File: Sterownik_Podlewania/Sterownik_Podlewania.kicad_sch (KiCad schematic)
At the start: 1 part, among them U1 ESP32-DEVKITC

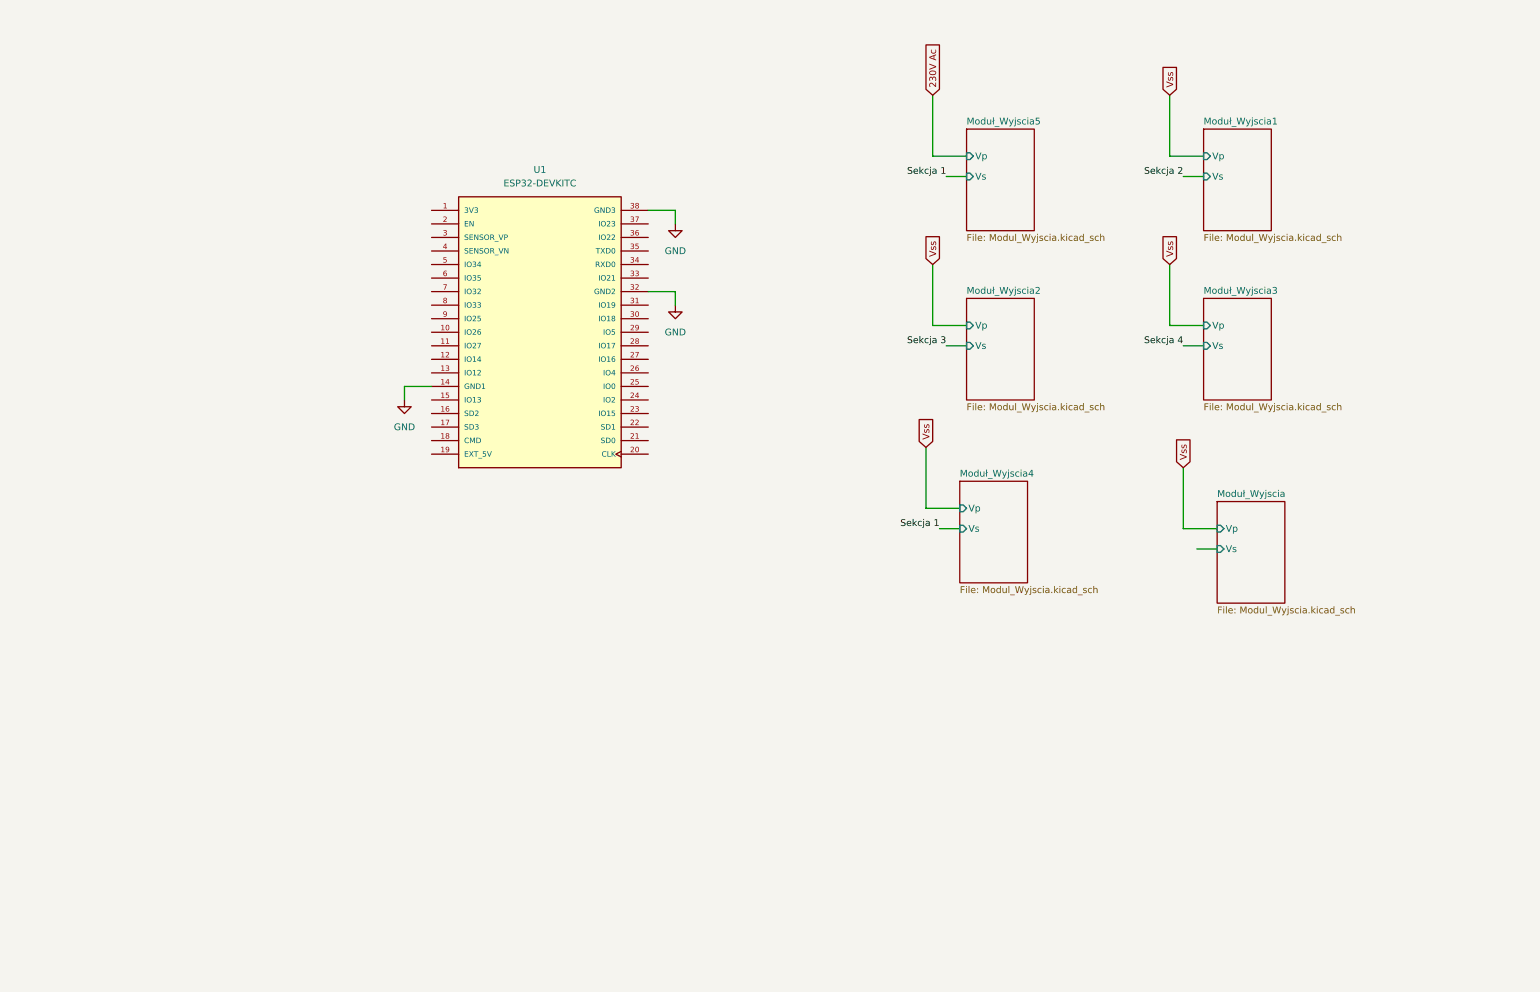
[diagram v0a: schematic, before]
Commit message: Dodanie zasilania, sekcji czujników światła, modyfikacja przełączników, dodanie znaczników
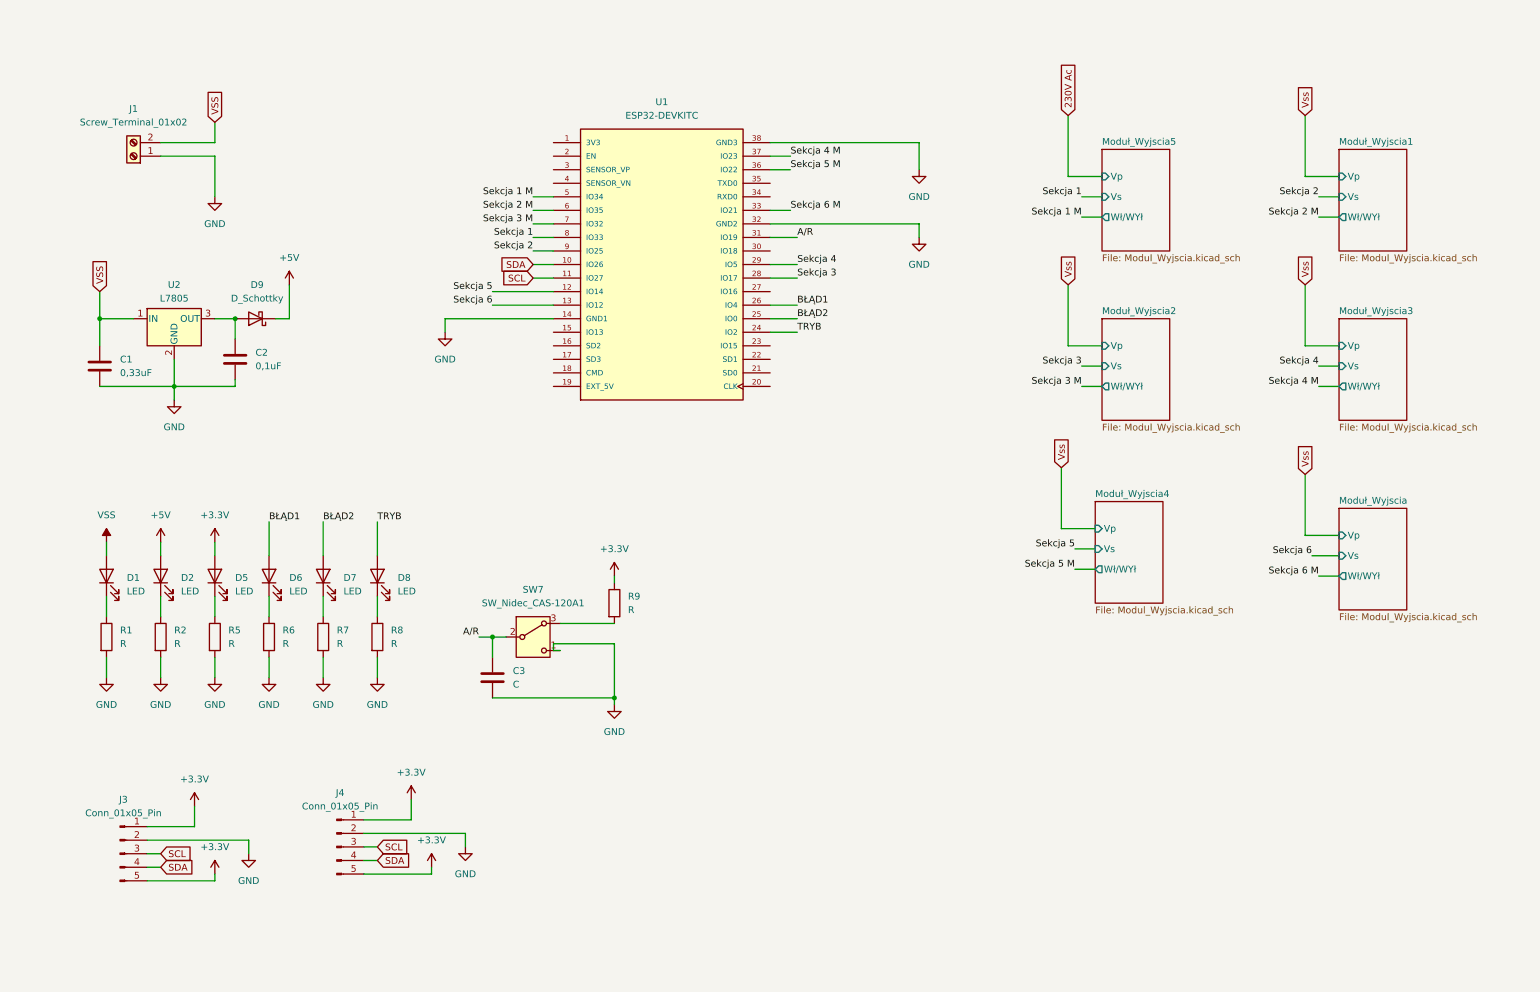
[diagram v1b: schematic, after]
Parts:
- added C1: 0,33uF, symbol Device:C
- added C2: 0,1uF, symbol Device:C
- added C3: C, symbol Device:C
- added D1, D2, D5, D6, D7, D8: LED, symbol Device:LED
- added D9: D_Schottky, symbol Device:D_Schottky
- added J1: Screw_Terminal_01x02, symbol Connector:Screw_Terminal_01x02
- added J3, J4: Conn_01x05_Pin, symbol Connector:Conn_01x05_Pin
- added R1, R2, R5, R6, R7, R8, R9: R, symbol Device:R
- added SW7: SW_Nidec_CAS-120A1, Button_Switch_SMD:Nidec_Copal_CAS-120A, symbol Switch:SW_Nidec_CAS-120A1
- added U2: L7805, symbol Regulator_Linear:L7805
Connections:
- net GND: now also C1.2, C2.2, C3.2, J1.1 (Pin_1), J3.2 (Pin_2), J4.2 (Pin_2), R1.2, R2.2, R5.2, R6.2, R7.2, R8.2, SW7.1 (C), U2.2 (GND)
- net Sekcja 1: now also U1.8 (IO33)
- net Sekcja 2: now also U1.9 (IO25)
- net Sekcja 3: now also U1.28 (IO17)
- net Sekcja 4: now also U1.29 (IO5)
- net SDA: now reaches U1.10 (IO26)
- net SDA: now also J3.4 (Pin_4), J4.4 (Pin_4)
- net SCL: now reaches U1.11 (IO27)
- net SCL: now also J3.3 (Pin_3), J4.3 (Pin_3)
- net Sekcja 5: now reaches U1.12 (IO14)
- net Sekcja 6: now reaches U1.13 (IO12)
- net TRYB: now reaches U1.24 (IO2)
- net TRYB: now also D8.2 (A)
- net BŁĄD2: now reaches U1.25 (IO0)
- net BŁĄD2: now also D7.2 (A)
- net BŁĄD1: now reaches U1.26 (IO4)
- net BŁĄD1: now also D6.2 (A)
- net A/R: now reaches U1.31 (IO19)
- net A/R: now also C3.1, SW7.2 (B)
- net Sekcja 6 M: now reaches U1.33 (IO21)
- net Sekcja 5 M: now reaches U1.36 (IO22)
- net Sekcja 4 M: now reaches U1.37 (IO23)
- net Sekcja 1 M: now reaches U1.5 (IO34)
- net Sekcja 2 M: now reaches U1.6 (IO35)
- net Sekcja 3 M: now reaches U1.7 (IO32)
- new net: D7.1 (K), R7.1
- new net: C2.1, D9.2 (A), U2.3 (OUT)
- new net: D2.1 (K), R2.1
- new net: D6.1 (K), R6.1
- new net: D5.1 (K), R5.1
- new net: R9.2, SW7.3 (A)
- new net: D8.1 (K), R8.1
- new net: D1.1 (K), R1.1
- new net +3.3V: D5.2 (A), J3.1 (Pin_1), J3.5 (Pin_5), J4.1 (Pin_1), J4.5 (Pin_5), R9.1
- new net +5V: D2.2 (A), D9.1 (K)
- new net VSS: C1.1, D1.2 (A), J1.2 (Pin_2), U2.1 (IN)
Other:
- sheet Moduł_Wyjscia ports: added Wł/WYł; removed none
- sheet Moduł_Wyjscia1 ports: added Wł/WYł; removed none
- sheet Moduł_Wyjscia2 ports: added Wł/WYł; removed none
- sheet Moduł_Wyjscia3 ports: added Wł/WYł; removed none
- sheet Moduł_Wyjscia4 ports: added Wł/WYł; removed none
- sheet Moduł_Wyjscia5 ports: added Wł/WYł; removed none
- moved on the sheet: U1

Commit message: Modyfikacja sekcji czujników
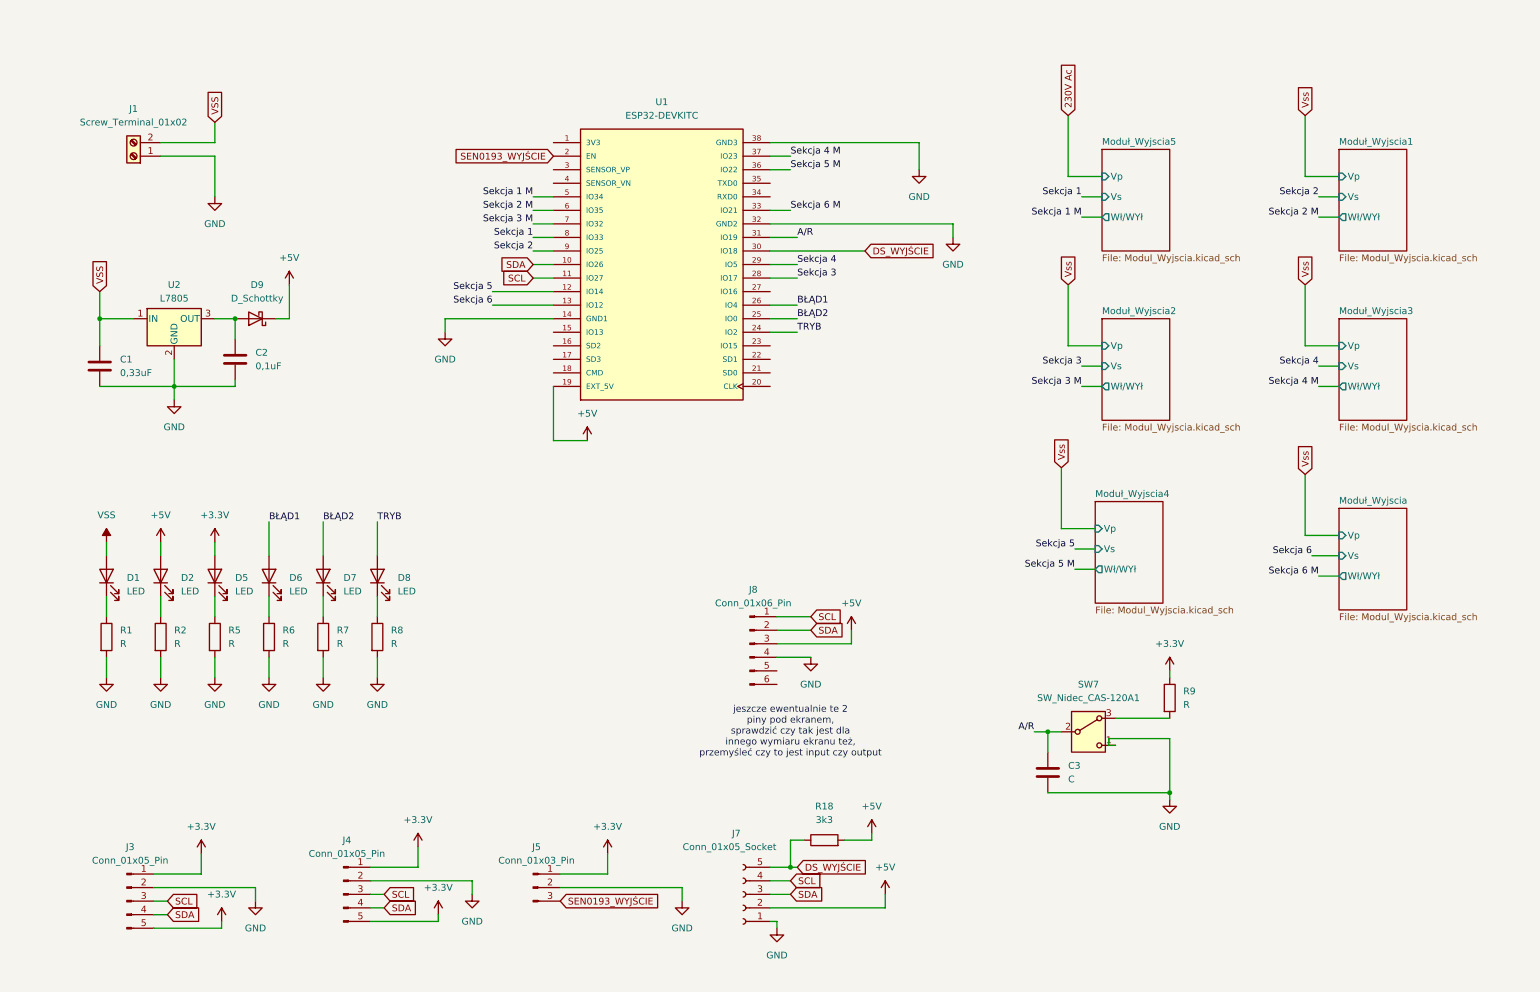
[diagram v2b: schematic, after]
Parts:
- added J5: Conn_01x03_Pin, symbol Connector:Conn_01x03_Pin
- added J7: Conn_01x05_Socket, symbol Connector:Conn_01x05_Socket
- added J8: Conn_01x06_Pin, symbol Connector:Conn_01x06_Pin
- added R18: 3k3, symbol Device:R
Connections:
- net +3.3V: now also J5.1 (Pin_1)
- net +5V: now also U1.19 (EXT_5V), J7.2 (Pin_2), J8.3 (Pin_3), R18.2
- net GND: now also J5.2 (Pin_2), J7.1 (Pin_1), J8.4 (Pin_4)
- net SCL: now also J7.4 (Pin_4), J8.1 (Pin_1)
- net SDA: now also J7.3 (Pin_3), J8.2 (Pin_2)
- net SEN0193_WYJŚCIE: now reaches U1.2 (EN)
- net SEN0193_WYJŚCIE: now also J5.3 (Pin_3)
- net DS_WYJŚCIE: now reaches U1.30 (IO18)
- net DS_WYJŚCIE: now also J7.5 (Pin_5), R18.1
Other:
- note added: "jeszcze ewentualnie te 2 piny pod ekranem, sprawdzić czy tak jest dla innego wymiaru ekranu też, przemyśleć czy to jest input czy output"
- moved on the sheet: C3, J3, J4, R9, SW7

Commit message: Dodanie adresów I2C, linków, czujnika temp, konwerter poziomów napięć
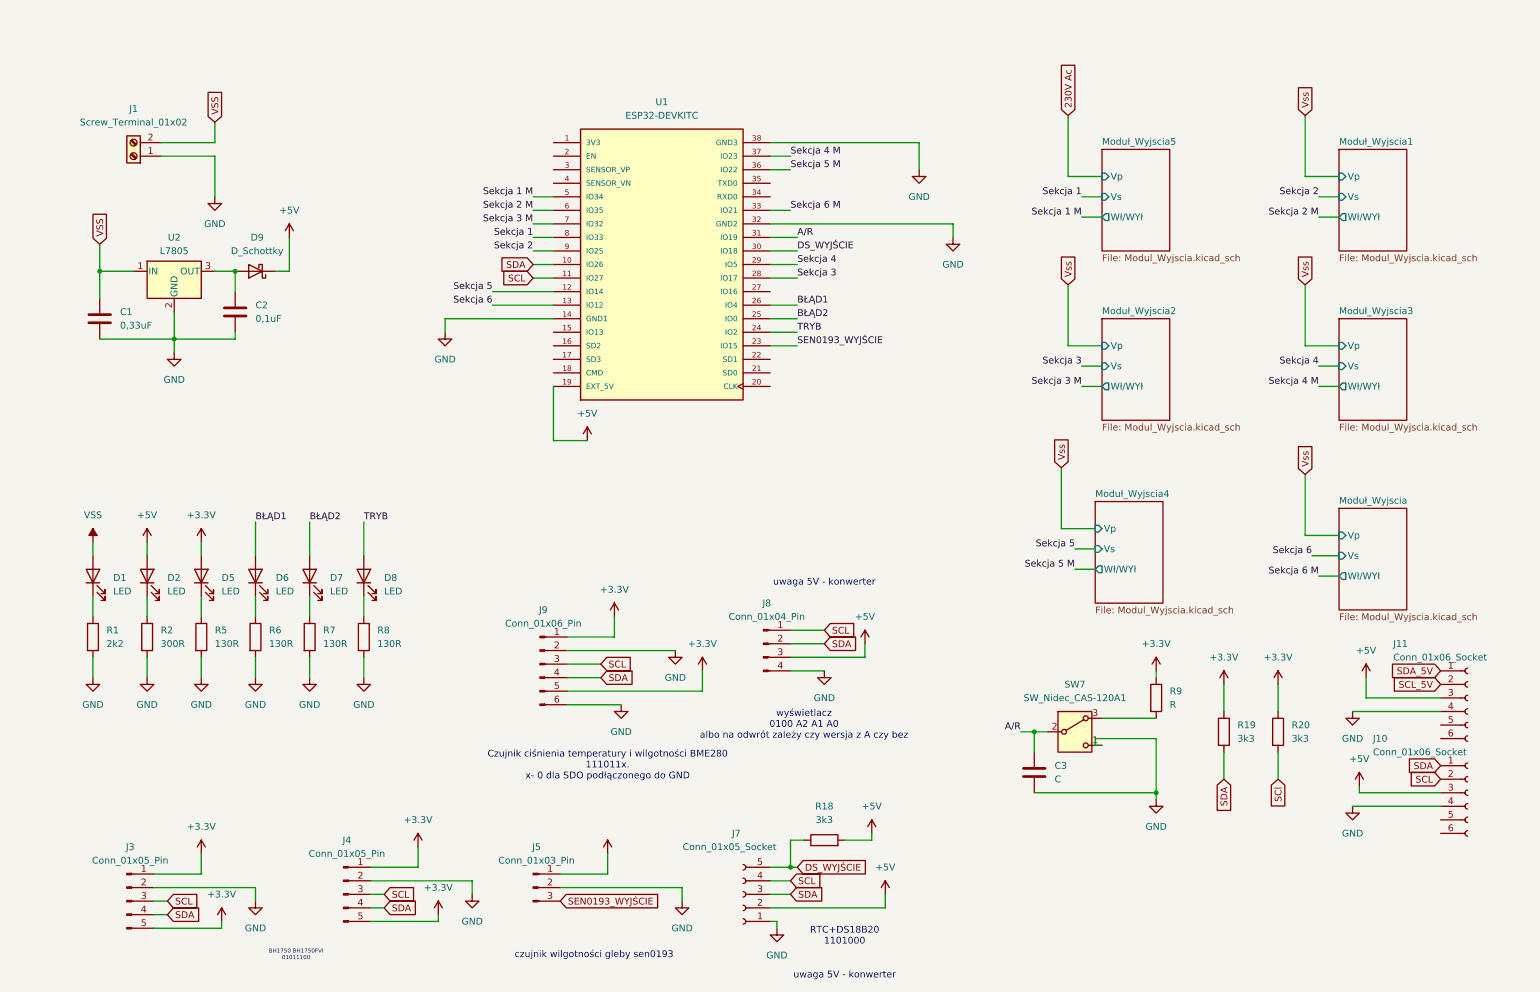
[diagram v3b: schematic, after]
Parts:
- removed J8: Conn_01x06_Pin, symbol Connector:Conn_01x06_Pin
- added J10, J11: Conn_01x06_Socket, symbol Connector:Conn_01x06_Socket
- added J8: Conn_01x04_Pin, symbol Connector:Conn_01x04_Pin
- added J9: Conn_01x06_Pin, symbol Connector:Conn_01x06_Pin
- added R19, R20: 3k3, symbol Device:R
- R1: value R -> 2k2
- R2: value R -> 300R
- R5, R6, R7, R8: value R -> 130R
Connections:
- net +3.3V: now also J9.1 (Pin_1), J9.5 (Pin_5), R19.1, R20.1
- net +5V: now also J10.3 (Pin_3), J11.3 (Pin_3), J8.3 (Pin_3)
- net GND: now also J10.4 (Pin_4), J11.4 (Pin_4), J8.4 (Pin_4), J9.2 (Pin_2), J9.6 (Pin_6)
- net SCL: now also J10.2 (Pin_2), J8.1 (Pin_1), J9.3 (Pin_3)
- net SDA: now also J10.1 (Pin_1), J8.2 (Pin_2), J9.4 (Pin_4), R19.2
- net SEN0193_WYJŚCIE: now also U1.23 (IO15); no longer U1.2 (EN)
- new net SCL_5V: J11.2 (Pin_2)
- new net SCl: R20.2
- new net SDA_5V: J11.1 (Pin_1)
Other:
- note added: "BH1750 BH1750FVI 01011100"
- note added: "Czujnik ciśnienia temperatury i wilgotności BME280 111011x. x- 0 dla SDO podłączonego do GND"
- note added: "RTC+DS18B20 1101000"
- note added: "czujnik wilgotności gleby sen0193"
- note added: "uwaga 5V - konwerter"
- note added: "wyświetlacz 0100 A2 A1 A0 albo na odwrót zależy czy wersja z A czy bez"
- note removed: "jeszcze ewentualnie te 2 piny pod ekranem, sprawdzić czy tak jest dla innego wymiaru ekranu też, przemyśleć czy to jest input czy output"
- moved on the sheet: C1, C2, C3, D1, D2, D5, D6, D7, D8, D9, R1, R2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
